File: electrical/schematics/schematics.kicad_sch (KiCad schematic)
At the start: 16 parts, among them SW101 , SW102 CHAVE MOTOR, SW103 

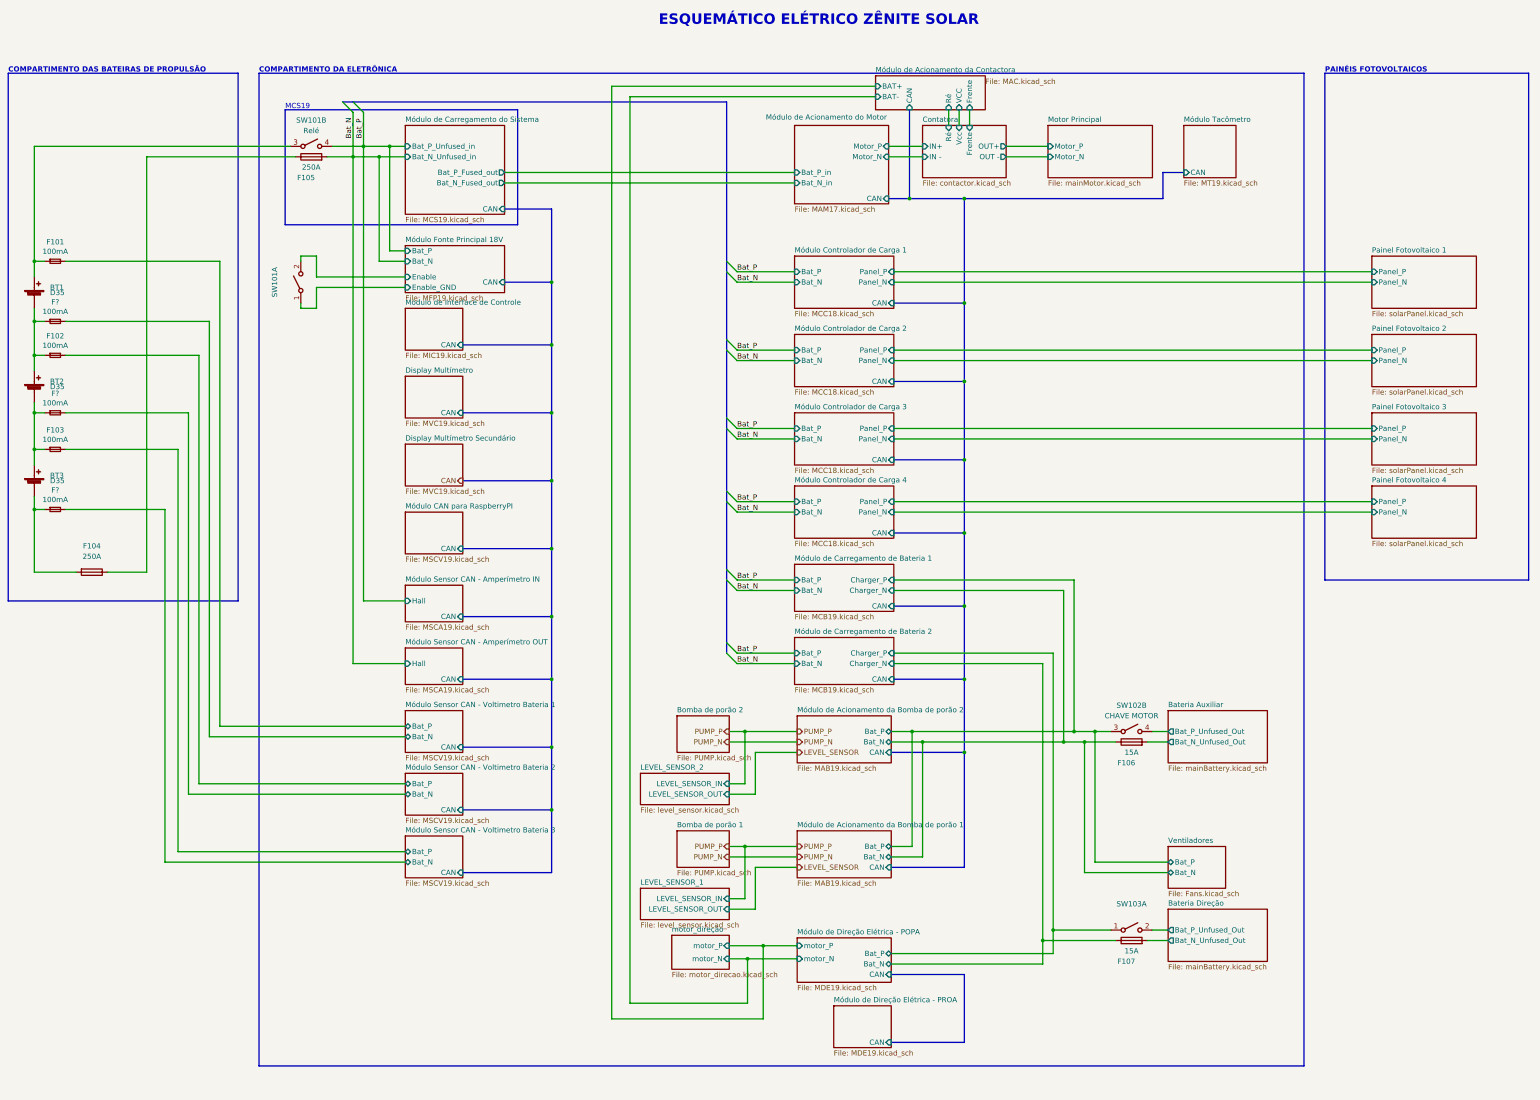
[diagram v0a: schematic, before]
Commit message: Esquematico revisado, agora mais limpo.
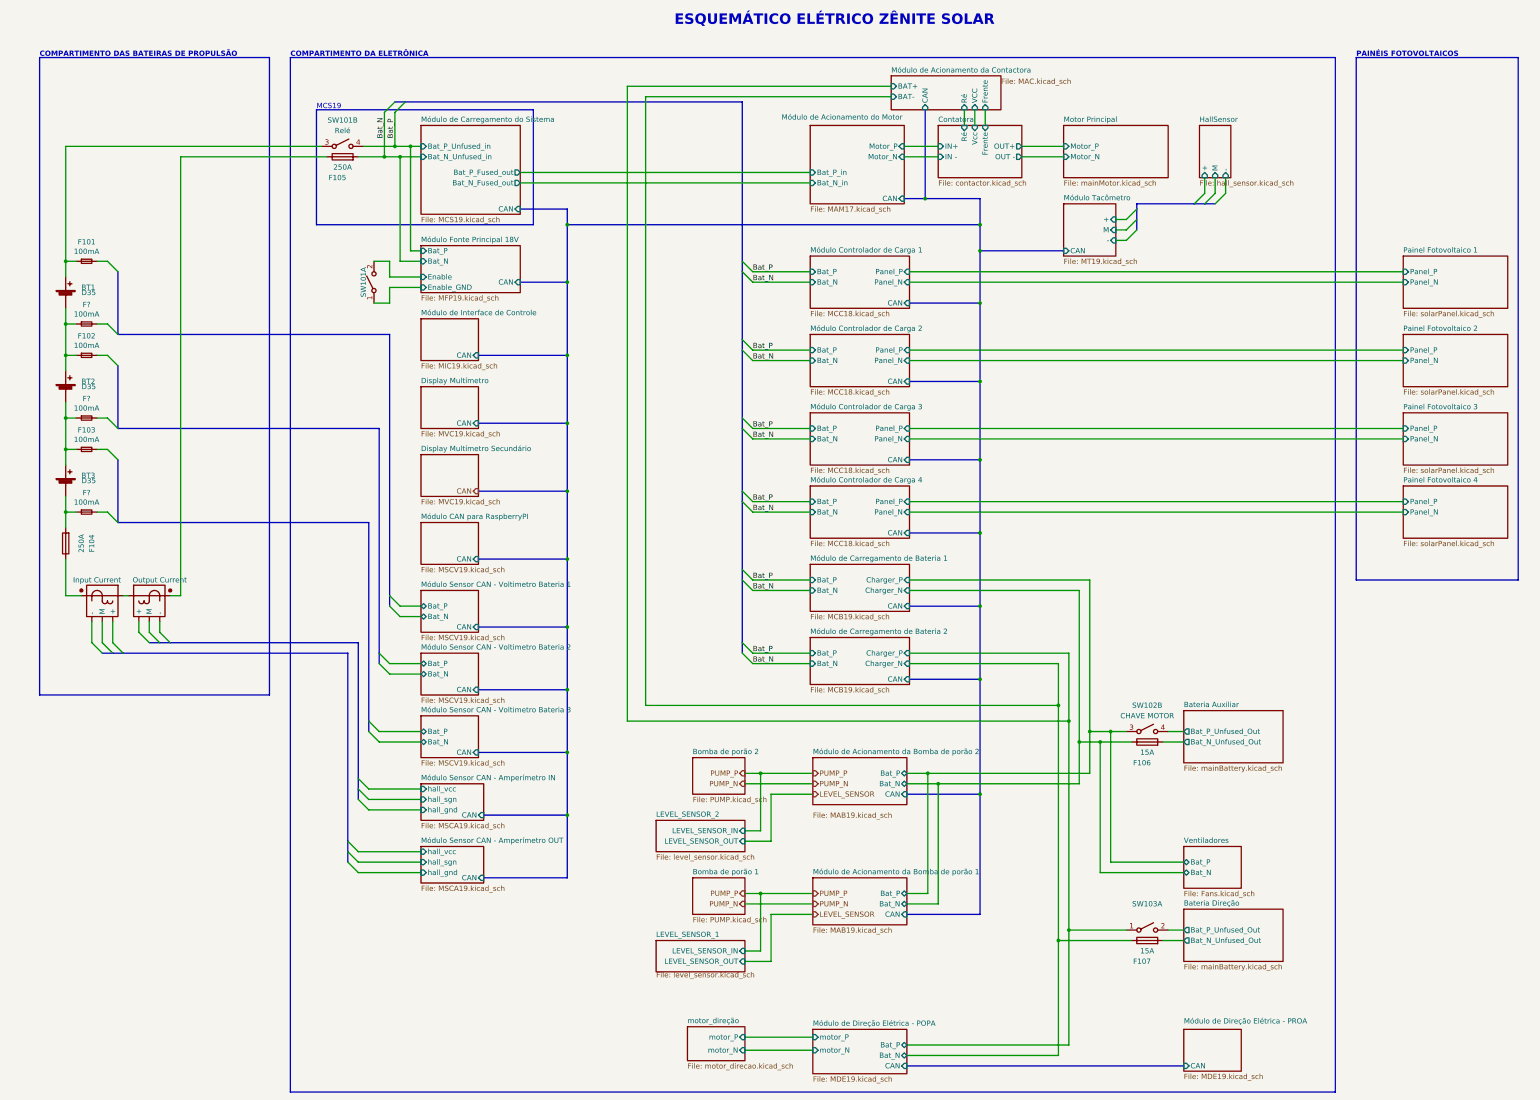
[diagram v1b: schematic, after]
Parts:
- added U?: Input Current, symbol New_Library:linear_coupler
- added U?: Output Current, symbol New_Library:linear_coupler
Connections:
- net Módulo de Carregamento de Bateria 2/Charger_N is gone; now on net Módulo de Acionamento da Contactora/BAT-: F107.1
- net Módulo de Carregamento de Bateria 2/Charger_P is gone; now on net Módulo de Acionamento da Contactora/BAT+: SW103.1 (A)
- net Módulo Sensor CAN - Voltimetro Bateria 1/Bat_N: no longer F?.2
- net Módulo Sensor CAN - Voltimetro Bateria 1/Bat_P: no longer F101.2
- net Módulo Sensor CAN - Voltimetro Bateria 2/Bat_N: no longer F?.2
- net Módulo Sensor CAN - Voltimetro Bateria 2/Bat_P: no longer F102.2
- net Módulo Sensor CAN - Voltimetro Bateria 3/Bat_N: no longer F?.2
- net Módulo Sensor CAN - Voltimetro Bateria 3/Bat_P: no longer F103.2
- net at F105.1: now also U?.2; no longer F104.1
- new net: F104.1, U?.2
- new net: U?.1, U?.1
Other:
- added sheet HallSensor (hall_sensor.kicad_sch)
- sheet Módulo Sensor CAN - Amperímetro IN ports: added hall_gnd, hall_sgn, hall_vcc; removed Hall
- sheet Módulo Sensor CAN - Amperímetro OUT ports: added hall_gnd, hall_sgn, hall_vcc; removed Hall
- sheet Módulo Tacômetro ports: added +, -, M; removed none
- moved on the sheet: BT1, BT2, BT3, F101, F102, F103, F104, F105, F106, F107, F?, SW101A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
